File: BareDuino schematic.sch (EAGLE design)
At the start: 33 parts, among them IC1 7805TV, X1 HC49-HC49-3L

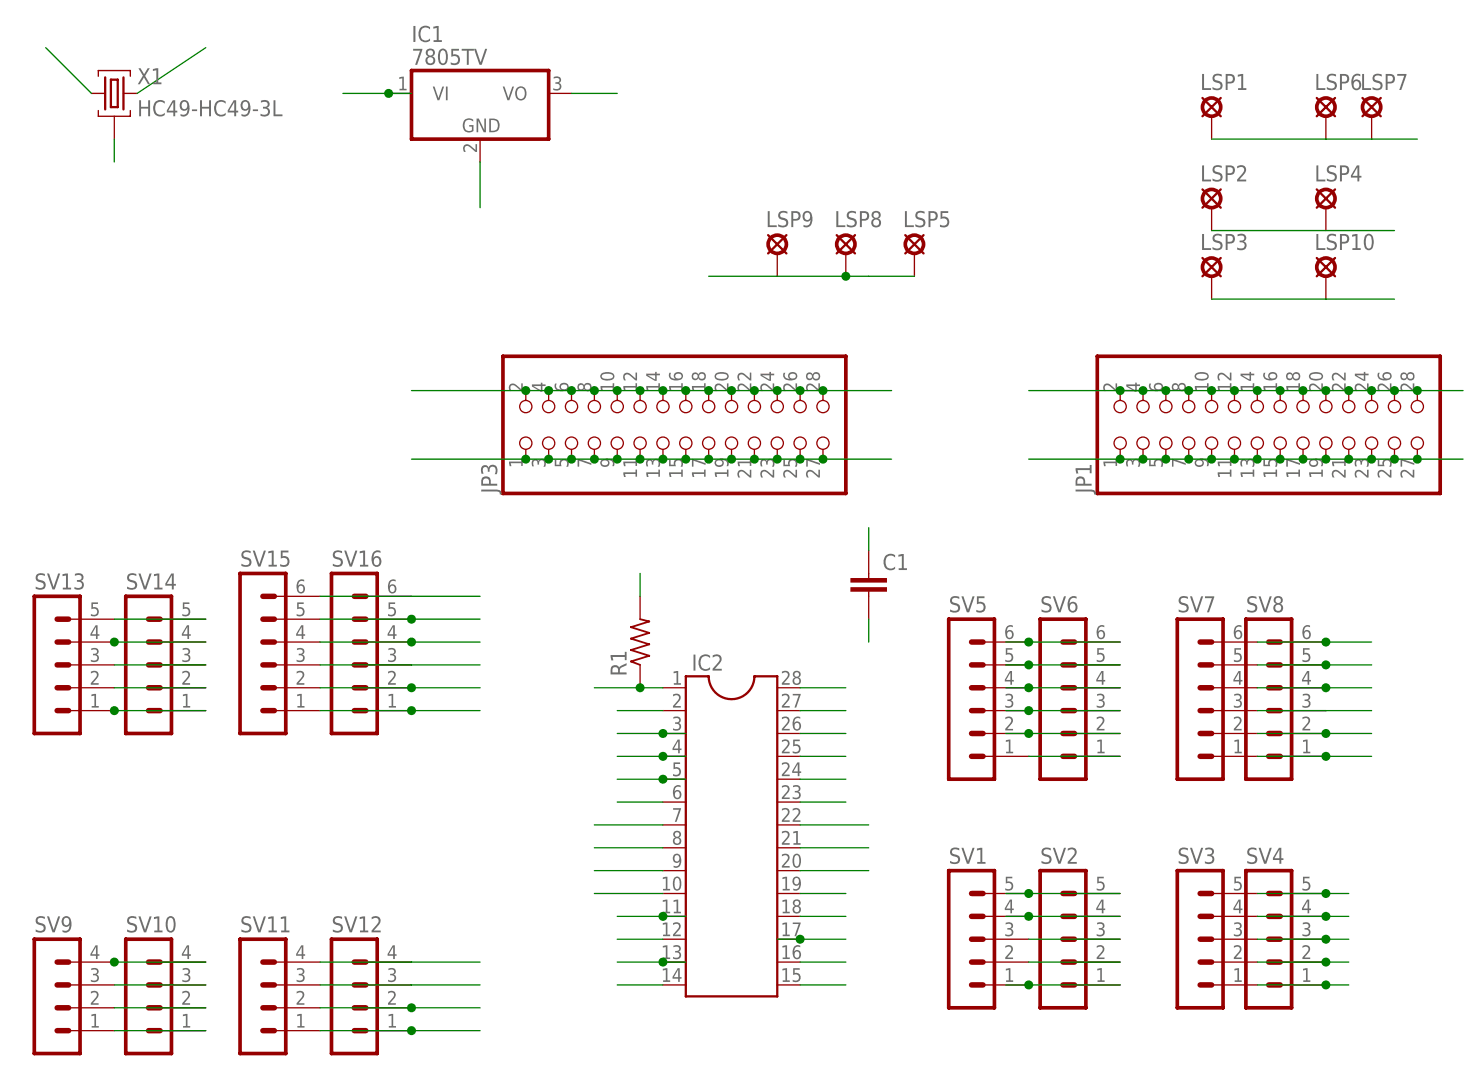
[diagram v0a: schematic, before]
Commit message: update! cleanup + servos + FTDI
fixes missing traces, realigns the breakout pads to make *all* of them
servo-friendly, adds an FTDI header, and adds labels on (most) pins
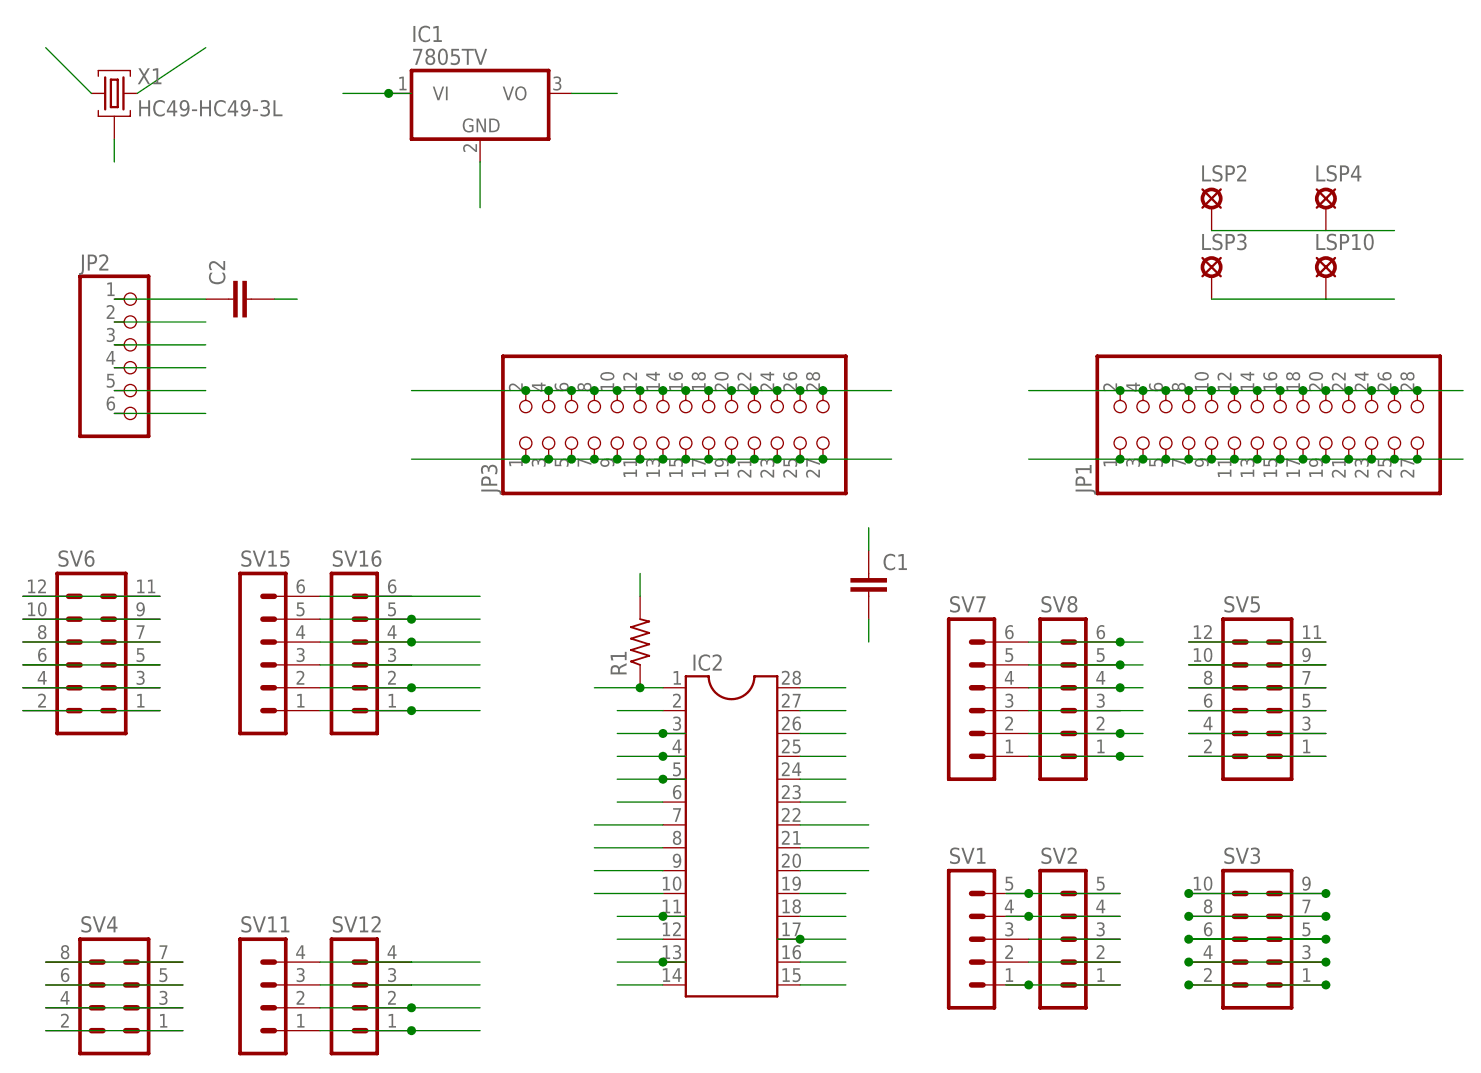
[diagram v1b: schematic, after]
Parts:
- removed LSP1, LSP5: SE14, solpad:SE14
- removed LSP6, LSP7, LSP8, LSP9: LSP10, solpad:LSP10
- removed SV10, SV9: (no value), con-lstb:MA04-1
- removed SV13, SV14: (no value), con-lstb:MA05-1
- added C2: (no value), capacitor-wima:C5/2.5
- added JP2: (no value), pinhead:PINHD-1X6
- R1: device resistor:R-US_0204/7 -> rcl:R-US_0204/5
- SV3: device con-lstb:MA05-1 -> con-lstb:MA05-2
- SV4: device con-lstb:MA05-1 -> con-lstb:MA04-2
- SV5, SV6: device con-lstb:MA06-1 -> con-lstb:MA06-2
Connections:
- removed net IO1: LSP1.MP, LSP6.MP, LSP7.MP
- removed net IO2: LSP5.MP, LSP8.MP, LSP9.MP
- new net N$21: C2.1, JP2.1
- new net N$22: SV6.1, SV6.2
- net DIP15: now also SV1.1, SV2.1; no longer SV3.1, SV4.1
- net DIP16: now also SV1.2, SV2.2; no longer SV3.2, SV4.2
- net DIP17: now also SV1.3, SV2.3; no longer SV3.3, SV4.3
- net DIP18: now also SV1.4, SV2.4; no longer SV3.4, SV4.4
- net DIP19: now also SV1.5, SV2.5; no longer SV3.5, SV4.5
- net DIP2: now also JP2.3
- net DIP3: now also JP2.2
- net GND: now also JP2.5, JP2.6
- net N$1: now also SV5.11, SV5.12; no longer SV5.6, SV6.6
- net N$10: now also SV4.1, SV4.2; no longer SV1.2, SV2.2
- net N$11: now also SV6.11, SV6.12; no longer SV1.1, SV2.1
- net N$12: now also SV3.5, SV3.6; no longer SV13.5, SV14.5
- net N$13: now also SV3.7, SV3.8; no longer SV13.4, SV14.4
- net N$14: now also SV3.10, SV3.9; no longer SV13.3, SV14.3
- net N$15: now also SV3.3, SV3.4; no longer SV13.2, SV14.2
- net N$16: now also SV3.1, SV3.2; no longer SV13.1, SV14.1
- net N$17: now also SV6.10, SV6.9; no longer SV10.4, SV9.4
- net N$18: now also SV6.7, SV6.8; no longer SV10.3, SV9.3
- net N$19: now also SV6.5, SV6.6; no longer SV10.2, SV9.2
- net N$2: now also SV5.10, SV5.9; no longer SV5.5, SV6.5
- net N$20: now also SV6.3, SV6.4; no longer SV10.1, SV9.1
- net N$3: now also SV5.7, SV5.8; no longer SV5.4, SV6.4
- net N$4: now also SV5.5, SV5.6; no longer SV5.3, SV6.3
- net N$5: now also SV5.3, SV5.4; no longer SV5.2, SV6.2
- net N$6: now also SV5.2; no longer SV6.1
- net N$7: now also SV4.7, SV4.8; no longer SV1.5, SV2.5
- net N$8: now also SV4.5, SV4.6; no longer SV1.4, SV2.4
- net N$9: now also SV4.3, SV4.4; no longer SV1.3, SV2.3
- net RST: now also C2.2
- net VCC: now also JP2.4
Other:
- moved on the sheet: SV7, SV8
